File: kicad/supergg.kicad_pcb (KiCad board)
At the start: 4 copper layers, 100 x 40 mm, 0 parts

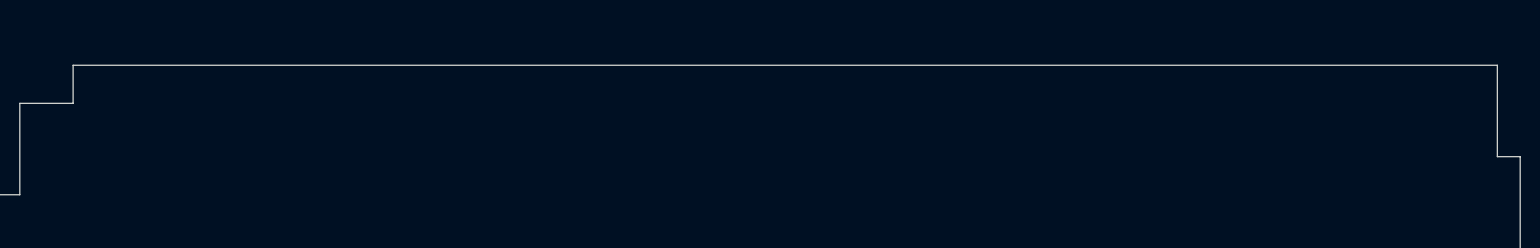
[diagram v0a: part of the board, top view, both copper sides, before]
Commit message: add pin connector holes
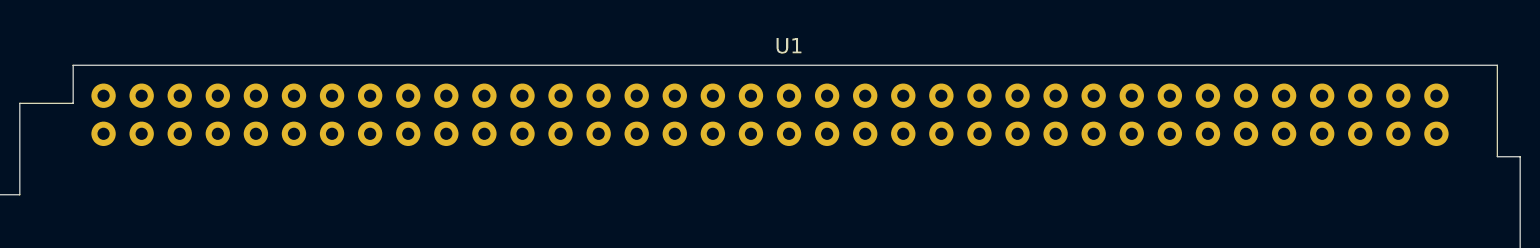
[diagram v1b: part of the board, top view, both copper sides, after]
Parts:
- added U1: Cart_Connector, supergg:Cart_Connector, F.Cu at (152.0, 88.5)

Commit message: add edge connector symbol
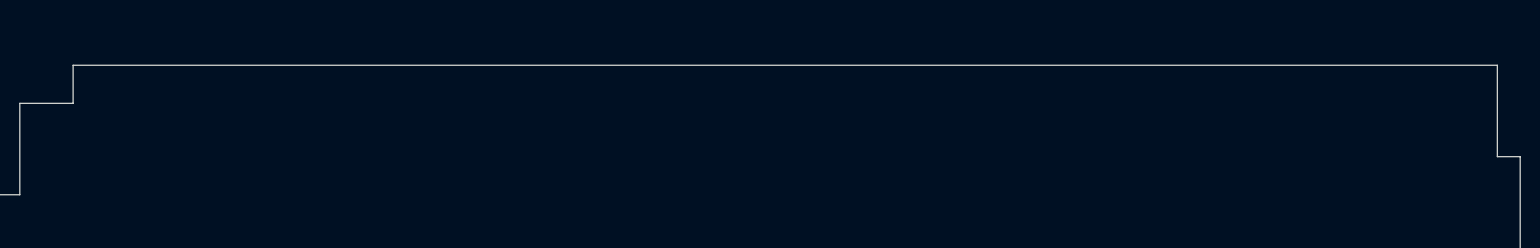
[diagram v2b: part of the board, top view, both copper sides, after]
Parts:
- removed U1: Cart_Connector, supergg:Cart_Connector

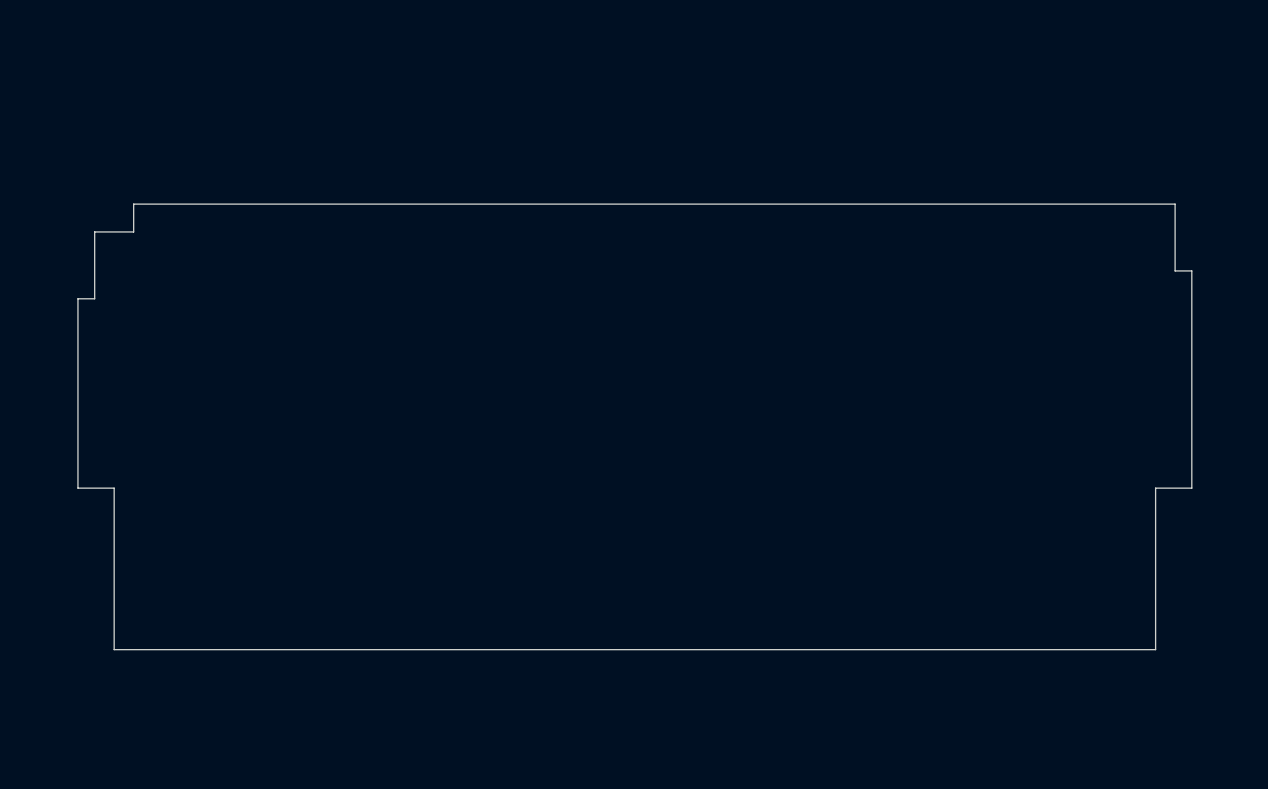
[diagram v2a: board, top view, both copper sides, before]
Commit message: add edge connector footprint
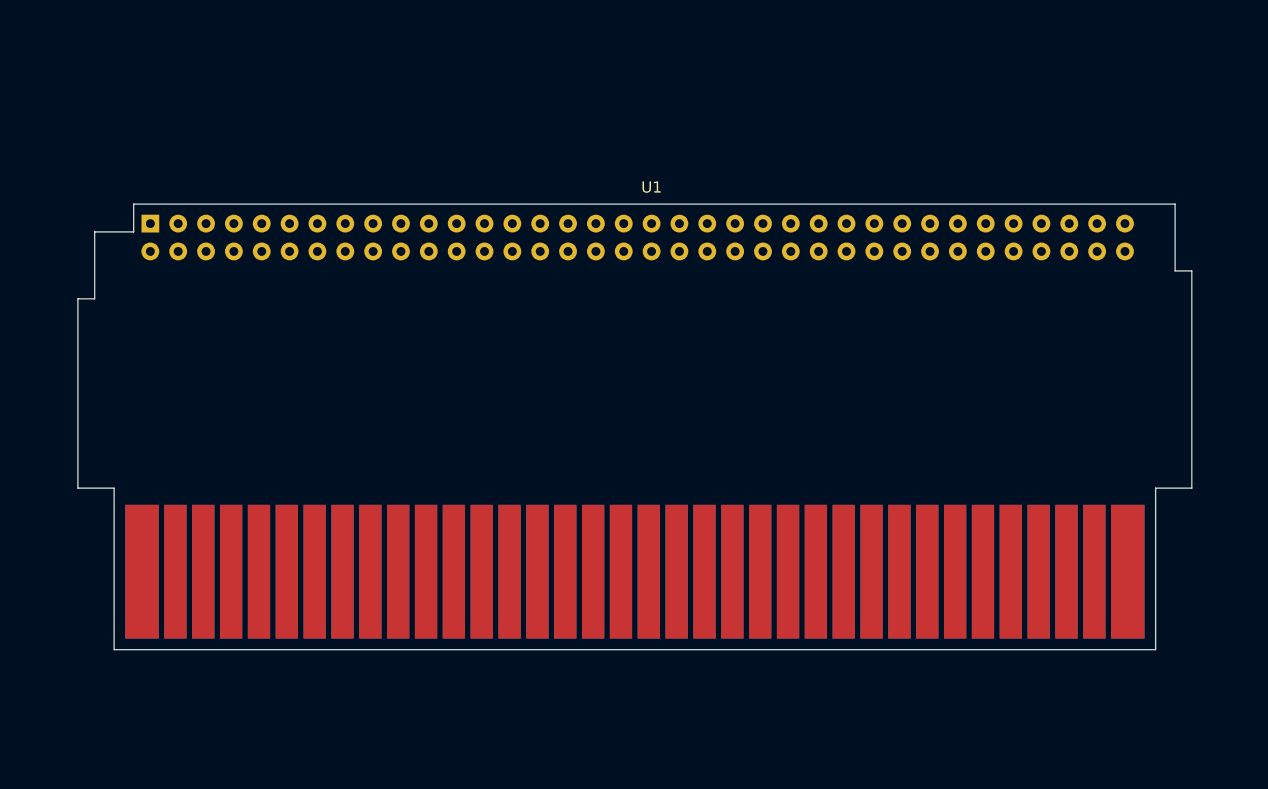
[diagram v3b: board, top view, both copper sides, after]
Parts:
- added U1: Pin_Connector, supergg:Pin_Connector, F.Cu at (151.5, 88.2)
- added U2: Edge_Connector, supergg:Edge_Connector, F.Cu at (150.0, 124.8)

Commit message: add symbols and footprints for most parts
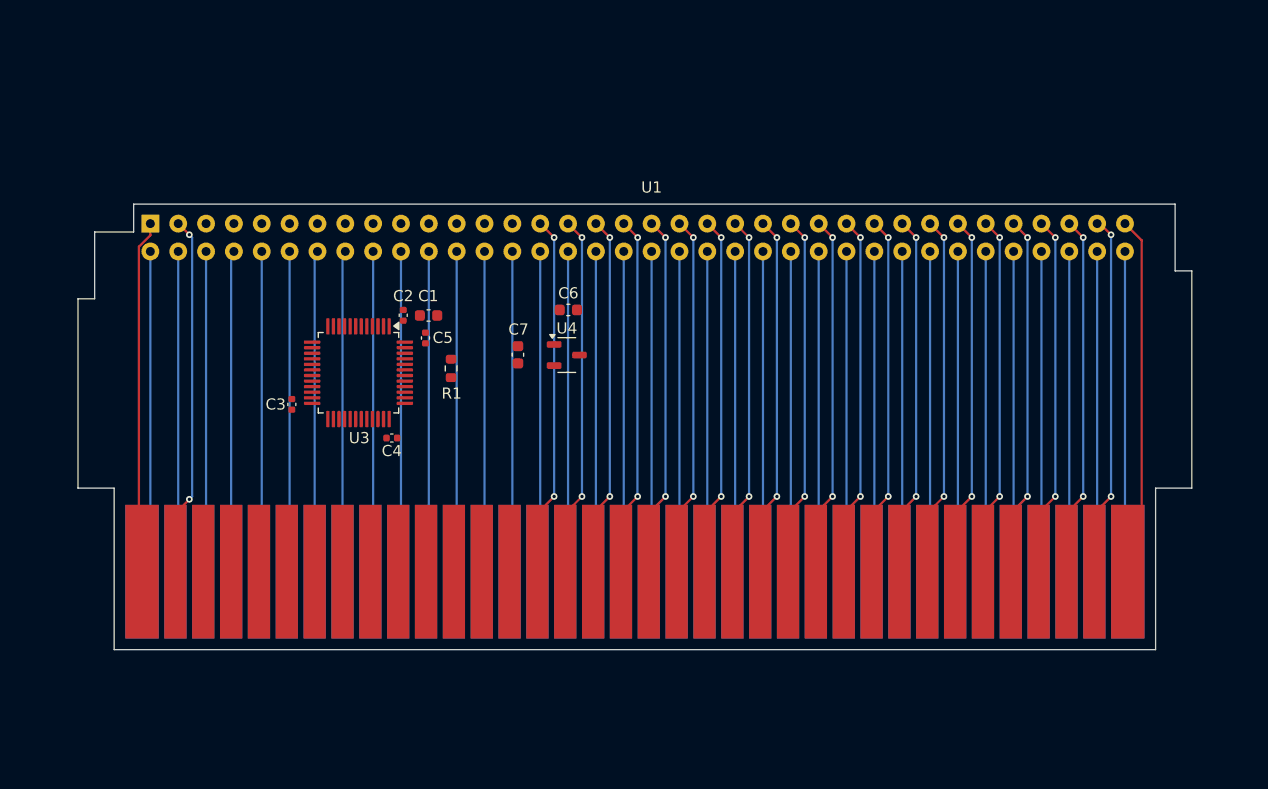
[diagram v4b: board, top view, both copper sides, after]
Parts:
- added C1: 4u7, Capacitor_SMD:C_0603_1608Metric, F.Cu at (131.5, 94.0)
- added C2: 100n, Capacitor_SMD:C_0402_1005Metric, F.Cu at (129.2, 94.0)
- added C3: 100n, Capacitor_SMD:C_0402_1005Metric, F.Cu at (119.2, 102.0)
- added C4: 100n, Capacitor_SMD:C_0402_1005Metric, F.Cu at (128.2, 105.0)
- added C5: 100n, Capacitor_SMD:C_0402_1005Metric, F.Cu at (131.2, 96.0)
- added C6: 1u, Capacitor_SMD:C_0603_1608Metric, F.Cu at (144.0, 93.5)
- added C7: 1u, Capacitor_SMD:C_0603_1608Metric, F.Cu at (139.5, 97.5)
- added R1: 10k, Resistor_SMD:R_0603_1608Metric, F.Cu at (133.5, 98.8)
- added U3: STM32F103C8Tx, Package_QFP:LQFP-48_7x7mm_P0.5mm, F.Cu at (125.2, 99.1)
- added U4: XC6206P332MR, Package_TO_SOT_SMD:SOT-23-3, F.Cu at (143.9, 97.5)
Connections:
- net /+5V renamed +5V
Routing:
- net /CIC_toMB: track 0.00 -> 32.5 mm, vias 0 -> 2
- net /EXP_2: track 0.00 -> 32.4 mm, vias 0 -> 2
- net /PPU_RD: track 0.00 -> 32.4 mm, vias 0 -> 2
- net /PPU_D3: track 0.00 -> 32.4 mm, vias 0 -> 2
- net /PPU_D2: track 0.00 -> 32.4 mm, vias 0 -> 2
- net /PPU_D1: track 0.00 -> 32.4 mm, vias 0 -> 2
- net /PPU_D0: track 0.00 -> 32.4 mm, vias 0 -> 2
- net /PPU_A6: track 0.00 -> 32.4 mm, vias 0 -> 2
- net /PPU_A5: track 0.00 -> 32.4 mm, vias 0 -> 2
- net /PPU_A4: track 0.00 -> 32.4 mm, vias 0 -> 2
- net /PPU_A3: track 0.00 -> 32.4 mm, vias 0 -> 2
- net /PPU_A2: track 0.00 -> 32.4 mm, vias 0 -> 2
- net /PPU_A1: track 0.00 -> 32.4 mm, vias 0 -> 2
- net /PPU_A0: track 0.00 -> 32.4 mm, vias 0 -> 2
- net /IRQ: track 0.00 -> 32.4 mm, vias 0 -> 2
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
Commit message: add wiring
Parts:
- moved U1 2.25 mm to (151.5, 86.0)
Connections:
- U1 pad 1: /GND_TOP -> GND
- U1 pad 72: /GND_BOT -> GND
- U2 pad 1: /GND_TOP -> GND
- U2 pad 72: /GND_BOT -> GND
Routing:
- net GND: track 0.00 -> 119.5 mm, vias 0 -> 1
- net +5V: track 32.4 -> 84.4 mm
- net /CPU_A11: track 32.4 -> 0.00 mm, vias 2 -> 0
- net /GND_TOP: track 31.8 -> 0.00 mm
- net /GND_BOT: track 28.9 -> 0.00 mm
- net /CPU_D7: track 28.9 -> 0.00 mm
- net /CPU_D6: track 28.9 -> 0.00 mm
- net /CPU_D5: track 28.9 -> 0.00 mm
- net /CPU_D4: track 28.9 -> 0.00 mm
- net /CPU_D3: track 28.9 -> 0.00 mm
- net /CPU_D2: track 28.9 -> 0.00 mm
- net /CPU_D1: track 28.9 -> 0.00 mm
- net /CPU_D0: track 28.9 -> 0.00 mm
- net /CPU_A14: track 28.9 -> 0.00 mm
- net /CPU_A13: track 28.9 -> 0.00 mm
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- added copper zone on B.Cu, net (none)
- added copper zone on F.Cu, net (none)

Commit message: rework wiring
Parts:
- added J1: Conn_01x04_Pin, Connector_PinHeader_2.54mm:PinHeader_1x04_P2.54mm_Horizontal, F.Cu at (189.1, 95.2)
- moved C1 47.3 mm to (178.8, 92.6)
- moved C2 47.3 mm to (176.5, 92.6)
- moved C4 47.3 mm to (175.5, 103.6)
- moved C5 47.3 mm to (178.5, 94.6)
- moved U3 47.3 mm to (172.5, 97.8)
- moved C3 47.3 mm to (166.5, 100.6)
- moved R1 46.1 mm to (179.6, 97.0), turned to 0 degrees
- moved C7 42.6 mm to (182.0, 94.8)
- moved U4 41.1 mm to (184.9, 94.8)
- moved C6 41.0 mm to (185.0, 92.2)
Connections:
- U3 pad 34: unconnected-(U3-PA13-Pad34) -> /SWDIO
- U3 pad 37: unconnected-(U3-PA14-Pad37) -> /SWDCLK
- U3 pad 39: unconnected-(U3-PB3-Pad39) -> /SWO
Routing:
- net +3.3V: track 7.39 -> 70.8 mm, vias 0 -> 2
- net +5V: track 84.4 -> 43.2 mm
- net /CPU_A12: track 0.00 -> 34.4 mm
- net /CPU_A11: track 0.00 -> 31.9 mm, vias 0 -> 2
- net /CPU_A10: track 0.00 -> 31.9 mm, vias 0 -> 2
- net /CPU_A14: track 0.00 -> 31.1 mm
- net /CPU_A13: track 0.00 -> 31.1 mm
- net /CPU_RW: track 0.00 -> 25.9 mm, vias 0 -> 2
- net /CPU_A9: track 0.00 -> 25.9 mm, vias 0 -> 2
- net /CPU_A8: track 0.00 -> 25.9 mm, vias 0 -> 2
- net /CPU_A7: track 0.00 -> 25.9 mm, vias 0 -> 2
- net /CPU_A6: track 0.00 -> 25.9 mm, vias 0 -> 2
- net /CPU_A5: track 0.00 -> 25.9 mm, vias 0 -> 2
- net /CPU_A4: track 0.00 -> 25.9 mm, vias 0 -> 2
- net /CPU_A3: track 0.00 -> 25.9 mm, vias 0 -> 2
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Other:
- board text added: "U2"

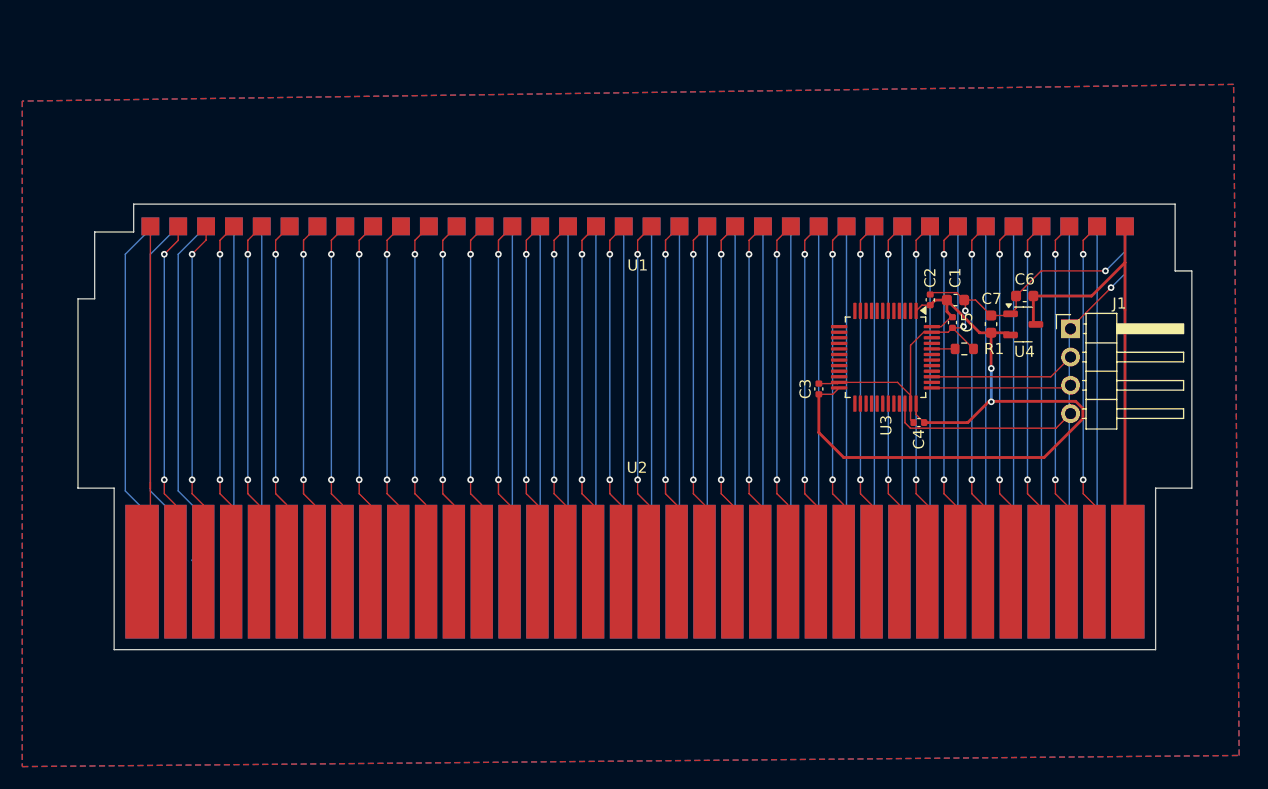
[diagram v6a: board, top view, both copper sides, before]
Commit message: finish first draft of wiring
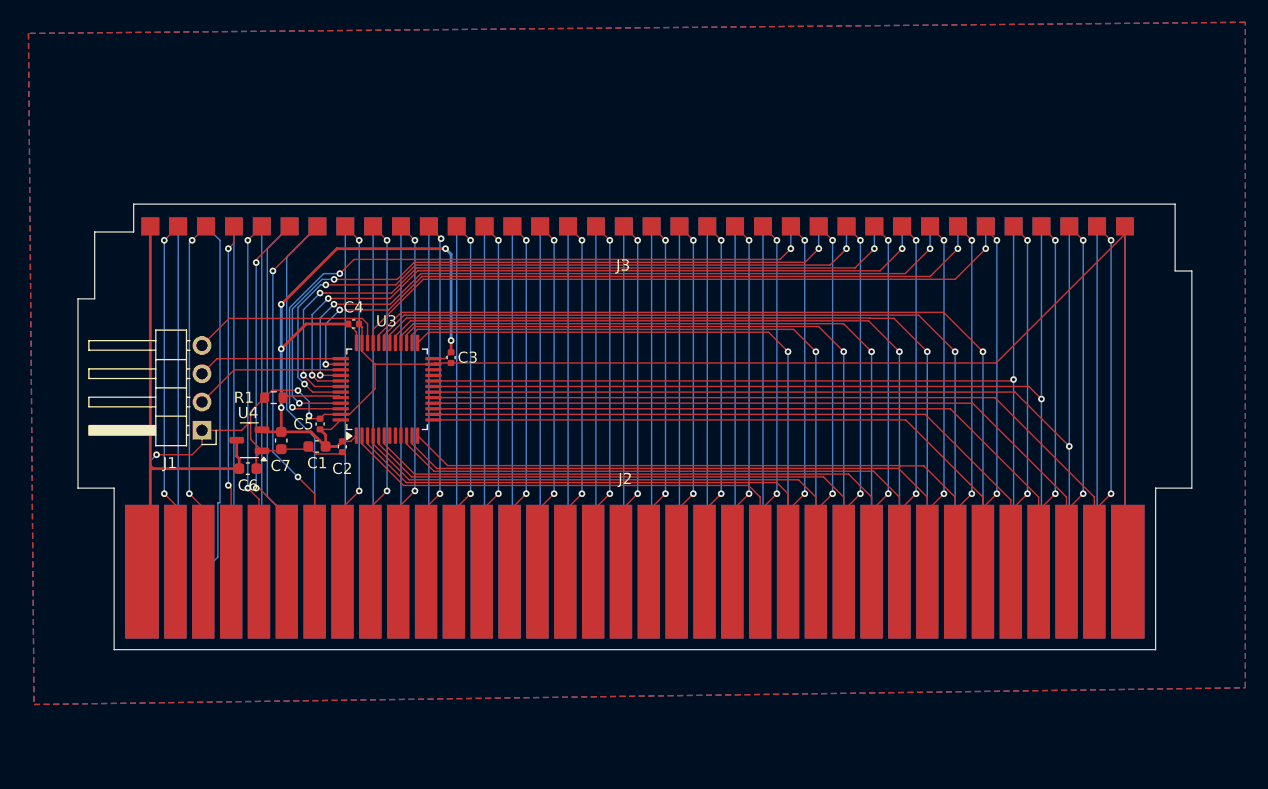
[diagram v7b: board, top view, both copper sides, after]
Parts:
- moved J1 78.5 mm to (111.1, 104.3), turned to 180 degrees
- moved C6 71.5 mm to (115.2, 107.8), turned to 0 degrees
- moved U4 70.2 mm to (115.4, 105.2), turned to 180 degrees
- moved C7 64.6 mm to (118.2, 105.2), turned to -90 degrees
- moved R1 62.2 mm to (117.6, 101.4), turned to 180 degrees
- moved C1 58.8 mm to (121.5, 105.8), turned to 180 degrees
- moved C5 57.5 mm to (121.7, 103.7), turned to 90 degrees
- moved C2 54.4 mm to (123.7, 105.8), turned to -90 degrees
- moved C4 51.5 mm to (124.8, 94.8), turned to 0 degrees
- moved U3 44.8 mm to (127.8, 100.6), turned to 90 degrees
- moved C3 33.1 mm to (133.5, 97.8), turned to -90 degrees
- moved J3 1.30 mm to (150.2, 86.0)
- moved J2 0.25 mm to (150.0, 124.5)
- renumbered U2 to J2, U1 to J3
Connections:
- J2 pad 42: /CPU_D7 -> /CPU_D7_edge
- J2 pad 43: /CPU_D6 -> /CPU_D6_edge
- J2 pad 44: /CPU_D5 -> /CPU_D5_edge
- J2 pad 45: /CPU_D4 -> /CPU_D4_edge
- J2 pad 46: /CPU_D3 -> /CPU_D3_edge
- J2 pad 47: /CPU_D2 -> /CPU_D2_edge
- J2 pad 48: /CPU_D1 -> /CPU_D1_edge
- J2 pad 49: /CPU_D0 -> /CPU_D0_edge
- J3 pad 42: /CPU_D7 -> /CPU_D7_pin
- J3 pad 43: /CPU_D6 -> /CPU_D6_pin
- J3 pad 44: /CPU_D5 -> /CPU_D5_pin
- J3 pad 45: /CPU_D4 -> /CPU_D4_pin
- J3 pad 46: /CPU_D3 -> /CPU_D3_pin
- J3 pad 47: /CPU_D2 -> /CPU_D2_pin
- J3 pad 48: /CPU_D1 -> /CPU_D1_pin
- J3 pad 49: /CPU_D0 -> /CPU_D0_pin
- U3 pad 10: unconnected-(U3-PA0-Pad10) -> /CPU_A4
- U3 pad 11: unconnected-(U3-PA1-Pad11) -> /CPU_A5
- U3 pad 12: unconnected-(U3-PA2-Pad12) -> /CPU_A6
- U3 pad 13: unconnected-(U3-PA3-Pad13) -> /CPU_A7
- U3 pad 14: unconnected-(U3-PA4-Pad14) -> /CPU_A8
- U3 pad 15: unconnected-(U3-PA5-Pad15) -> /CPU_A9
- U3 pad 16: unconnected-(U3-PA6-Pad16) -> /CPU_A10
- U3 pad 17: unconnected-(U3-PA7-Pad17) -> /CPU_A11
- U3 pad 18: unconnected-(U3-PB0-Pad18) -> /CPU_A12
- U3 pad 19: unconnected-(U3-PB1-Pad19) -> /CPU_A13
- U3 pad 2: unconnected-(U3-PC13-Pad2) -> /CPU_RW
- U3 pad 20: unconnected-(U3-PB2-Pad20) -> /CPU_A14
- U3 pad 25: unconnected-(U3-PB12-Pad25) -> /CPU_D0_edge
- U3 pad 26: unconnected-(U3-PB13-Pad26) -> /CPU_D1_edge
- U3 pad 27: unconnected-(U3-PB14-Pad27) -> /CPU_D2_edge
- U3 pad 28: unconnected-(U3-PB15-Pad28) -> /CPU_D3_edge
- U3 pad 29: unconnected-(U3-PA8-Pad29) -> /CPU_D4_edge
- U3 pad 3: unconnected-(U3-PC14-Pad3) -> /CPU_A0
- U3 pad 30: unconnected-(U3-PA9-Pad30) -> /CPU_D5_edge
- U3 pad 31: unconnected-(U3-PA10-Pad31) -> /CPU_D6_edge
- U3 pad 32: unconnected-(U3-PA11-Pad32) -> /CPU_D7_edge
- U3 pad 33: unconnected-(U3-PA12-Pad33) -> /CPU_D7_pin
- U3 pad 38: unconnected-(U3-PA15-Pad38) -> /CPU_D6_pin
- U3 pad 4: unconnected-(U3-PC15-Pad4) -> /CPU_A1
- U3 pad 40: unconnected-(U3-PB4-Pad40) -> /CPU_D5_pin
- U3 pad 41: unconnected-(U3-PB5-Pad41) -> /CPU_D4_pin
- U3 pad 42: unconnected-(U3-PB6-Pad42) -> /CPU_D3_pin
- U3 pad 43: unconnected-(U3-PB7-Pad43) -> /CPU_D2_pin
- U3 pad 45: unconnected-(U3-PB8-Pad45) -> /CPU_D1_pin
- U3 pad 46: unconnected-(U3-PB9-Pad46) -> /CPU_D0_pin
- U3 pad 5: unconnected-(U3-PD0-Pad5) -> /CPU_A2
- U3 pad 6: unconnected-(U3-PD1-Pad6) -> /CPU_A3
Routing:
- net /CPU_D7_edge: track 0.00 -> 77.0 mm, vias 0 -> 1
- net /CPU_D6_edge: track 0.00 -> 73.8 mm, vias 0 -> 1
- net /CPU_D5_edge: track 0.00 -> 70.6 mm, vias 0 -> 1
- net /CPU_A11: track 31.9 -> 101.9 mm
- net /CPU_D4_edge: track 0.00 -> 67.3 mm, vias 0 -> 1
- net /CPU_D6_pin: track 0.00 -> 66.5 mm, vias 0 -> 3
- net /CPU_D5_pin: track 0.00 -> 66.3 mm, vias 0 -> 3
- net /CPU_D4_pin: track 0.00 -> 65.6 mm, vias 0 -> 3
- net /CPU_D3_pin: track 0.00 -> 65.2 mm, vias 0 -> 3
- net /CPU_A9: track 25.9 -> 91.0 mm
- net /CPU_D3_edge: track 0.00 -> 64.1 mm, vias 0 -> 1
- net /CPU_D2_pin: track 0.00 -> 64.1 mm, vias 0 -> 3
- net /CPU_D1_pin: track 0.00 -> 63.9 mm, vias 0 -> 3
- net /CPU_D0_pin: track 0.00 -> 62.6 mm, vias 0 -> 3
- net /CPU_A8: track 25.9 -> 88.1 mm
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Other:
- board text added: "J2"
- board text removed: "U2"
